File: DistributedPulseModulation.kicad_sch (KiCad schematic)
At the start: 43 parts, among them J1 Conn_02x12_Odd_Even, J2 Conn_02x05_Odd_Even, U1 74LS251, U10 4053, U11 4053, U12 4053, U2 74LVC2G74, U25 74LS85, U28 74LS85, U31 74LS85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

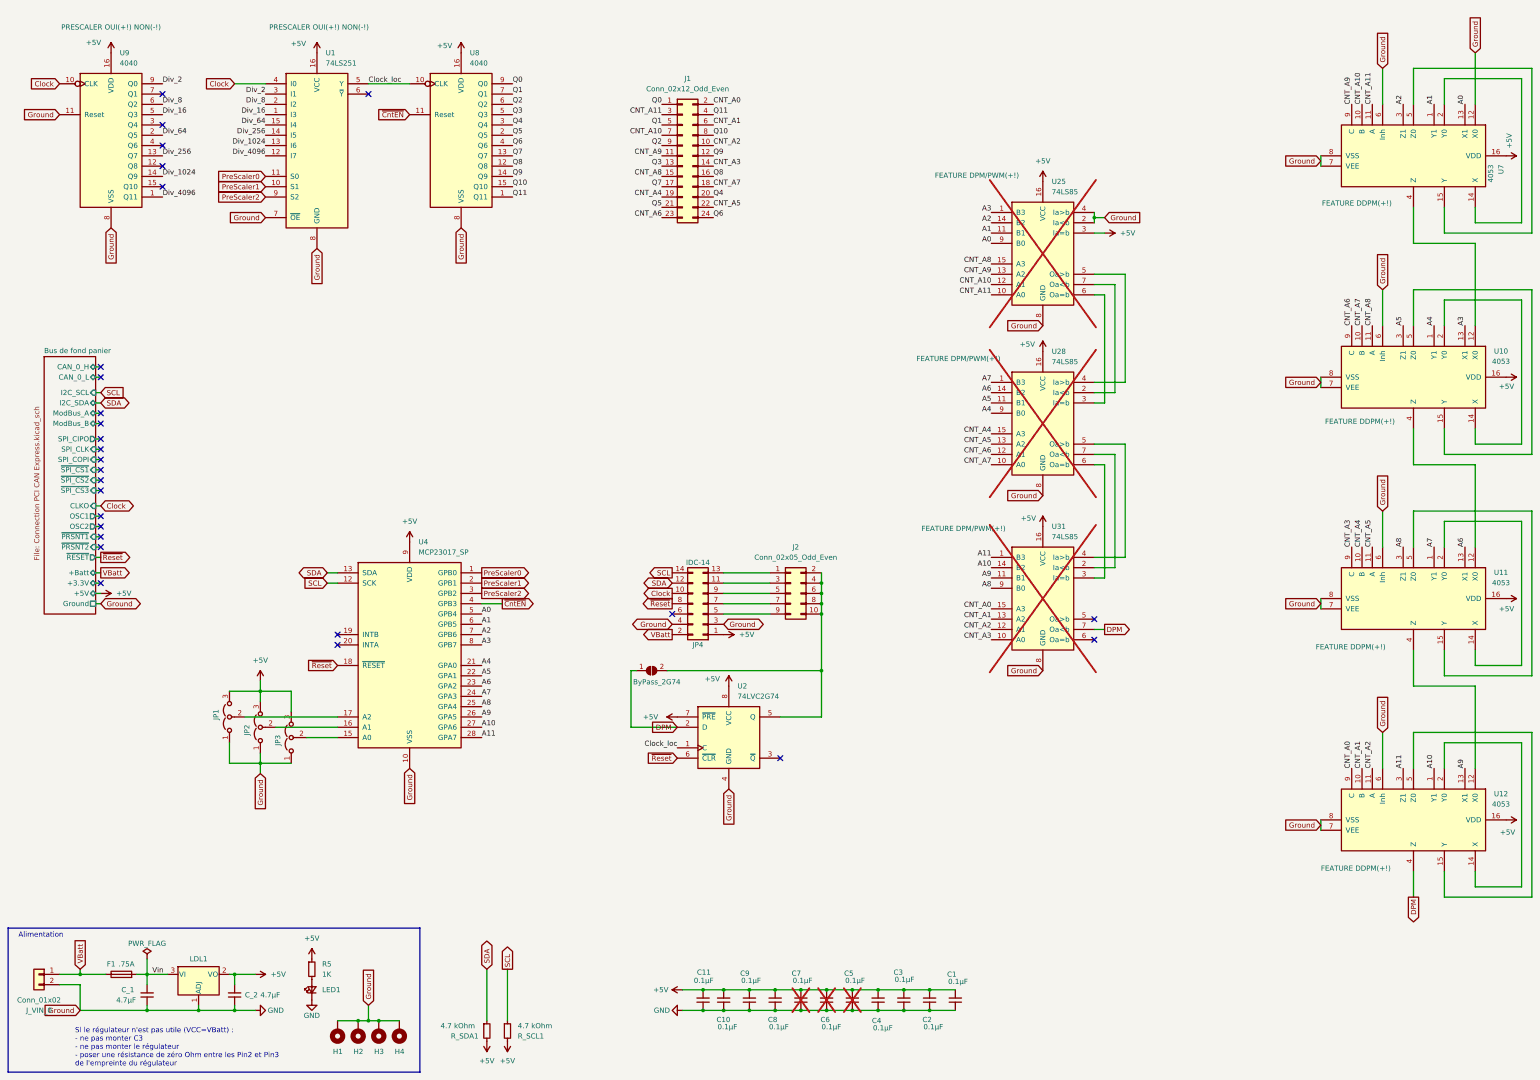
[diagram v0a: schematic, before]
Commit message: Feature : - DPM et DDPM sur même position de jumper - PWM sur jumpers en croisés
KiVar :
- création des 4 aspects FULL, PWM, DPM et DDPM

Doc/img :
- mise à jour du README.md
- mise à jour des screeshots
- intégration directe dans le projet des modèles 3D
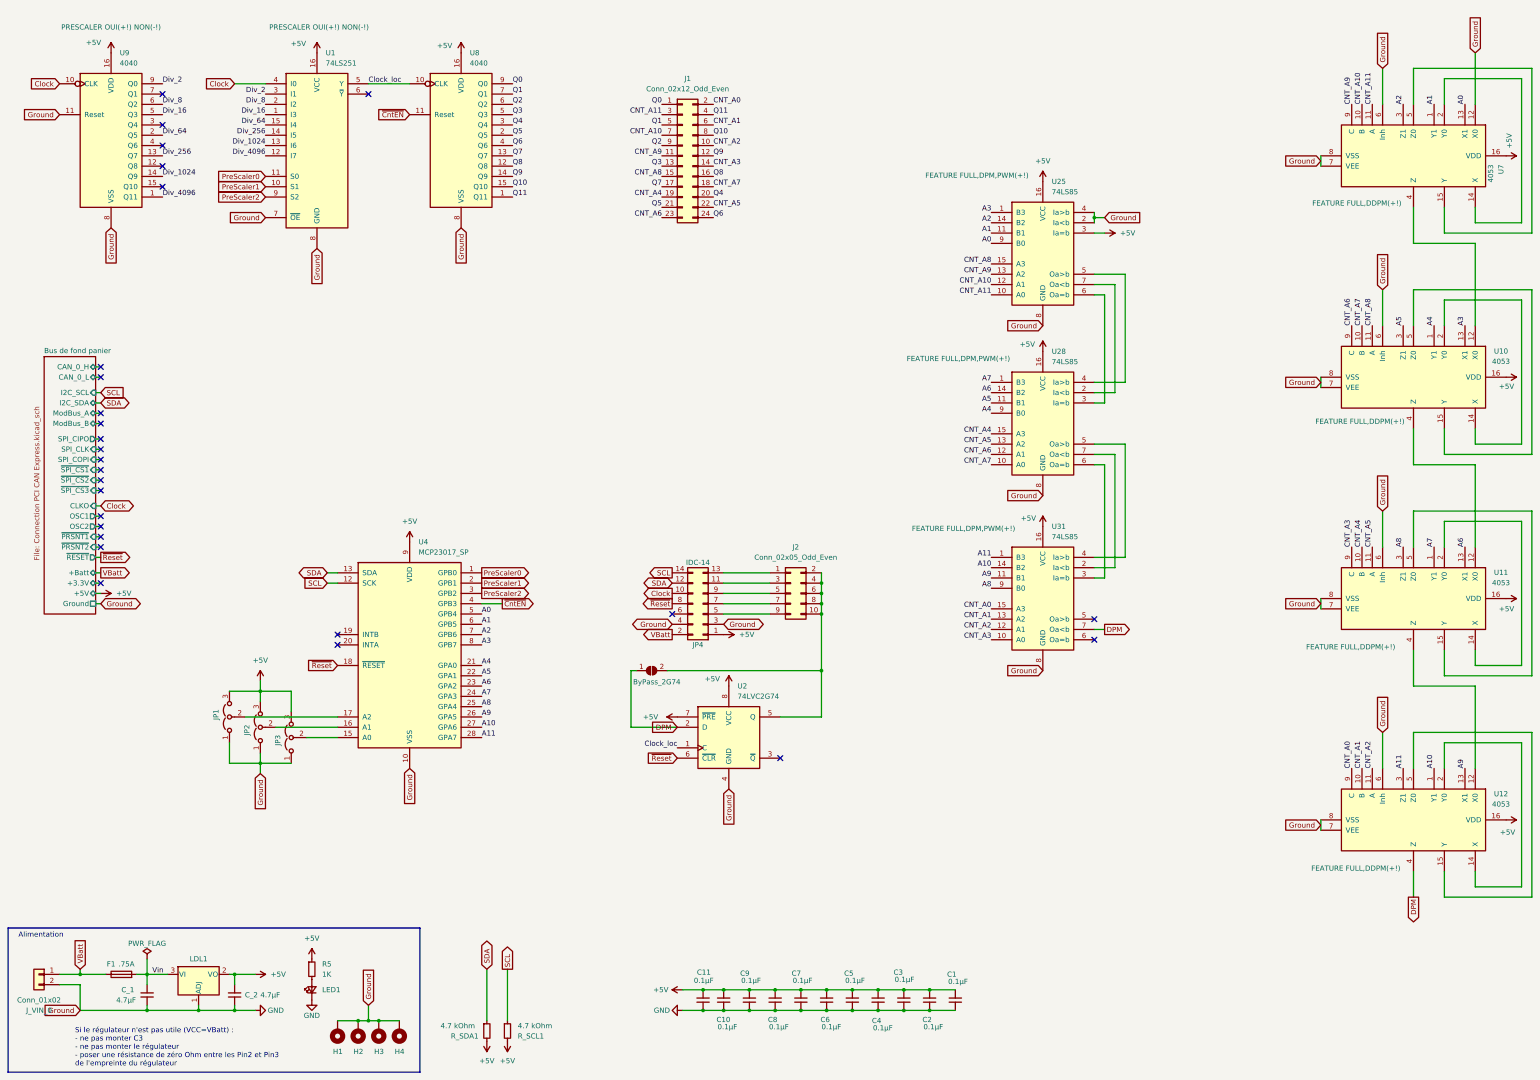
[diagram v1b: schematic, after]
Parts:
- C10, C11, C8, C9, U10, U11, U12, U7: Var FEATURE DDPM(+!) -> FEATURE FULL,DDPM(+!)
- C5, C6, C7, U25, U28, U31: Var FEATURE DPM/PWM(+!) -> FEATURE FULL,DPM,PWM(+!); now fitted; now in the parts list
- J1: Var (none) -> FEATURE FULL(+m1) DDPM,DPM(+m2) PWM(+m3)

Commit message: Travaux préparatoire : V2.0 - Ajout jumper Dyadic vs P82C150 - B.Silkscreen major update
TODO :
- Suppression connecteur IDC
- Ajout pinheader horizontal pour les 5 outputs
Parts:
- added JP5: Jumper_3_Open, Connector_PinHeader_2.54mm:PinHeader_1x03_P2.54mm_Vertical, symbol Jumper:Jumper_3_Open
- J1: Var FEATURE FULL(+m1) DDPM,DPM(+m2) PWM(+m3) -> FEATURE PWM(+m1) FULL,DDPM,DPM(+m2)
- J_VIN_0: footprint Connector_PinHeader_2.54mm:PinHeader_1x02_P2.54mm_Vertical -> TerminalBlock_TE-Connectivity:TerminalBlock_TE_282834-2_1x02_P2.54mm_Horizontal
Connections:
- net DPM: no longer names the net of ByPass_2G74.1 (A), U2.2 (D)
- net DPM: now also JP5.2 (C); no longer U12.4 (Z), U31.7 (Oa<b)
- new net DDPM: JP5.1 (A), U12.4 (Z)
- new net DPM_PWM: JP5.3 (B), U31.7 (Oa<b)

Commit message: Pré-version de la v2.0
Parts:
- removed J2: Conn_02x05_Odd_Even, Connector_PinHeader_2.54mm:PinHeader_2x05_P2.54mm_Vertical, symbol Connector_Generic:Conn_02x05_Odd_Even
- removed JP4: IDC-14, Connector_IDC:IDC-Header_2x07_P2.54mm_Horizontal, symbol Connector_Generic:Conn_02x07_Odd_Even
- added J2: Conn_01x01, Connector_PinSocket_2.54mm:PinSocket_1x01_P2.54mm_Horizontal, symbol Connector_Generic:Conn_01x01
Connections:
- net DPM: now reaches ByPass_2G74.2 (B), U2.5 (Q)
- net DPM: now also J2.1 (Pin_1)
- no-connect marks 27 -> 26

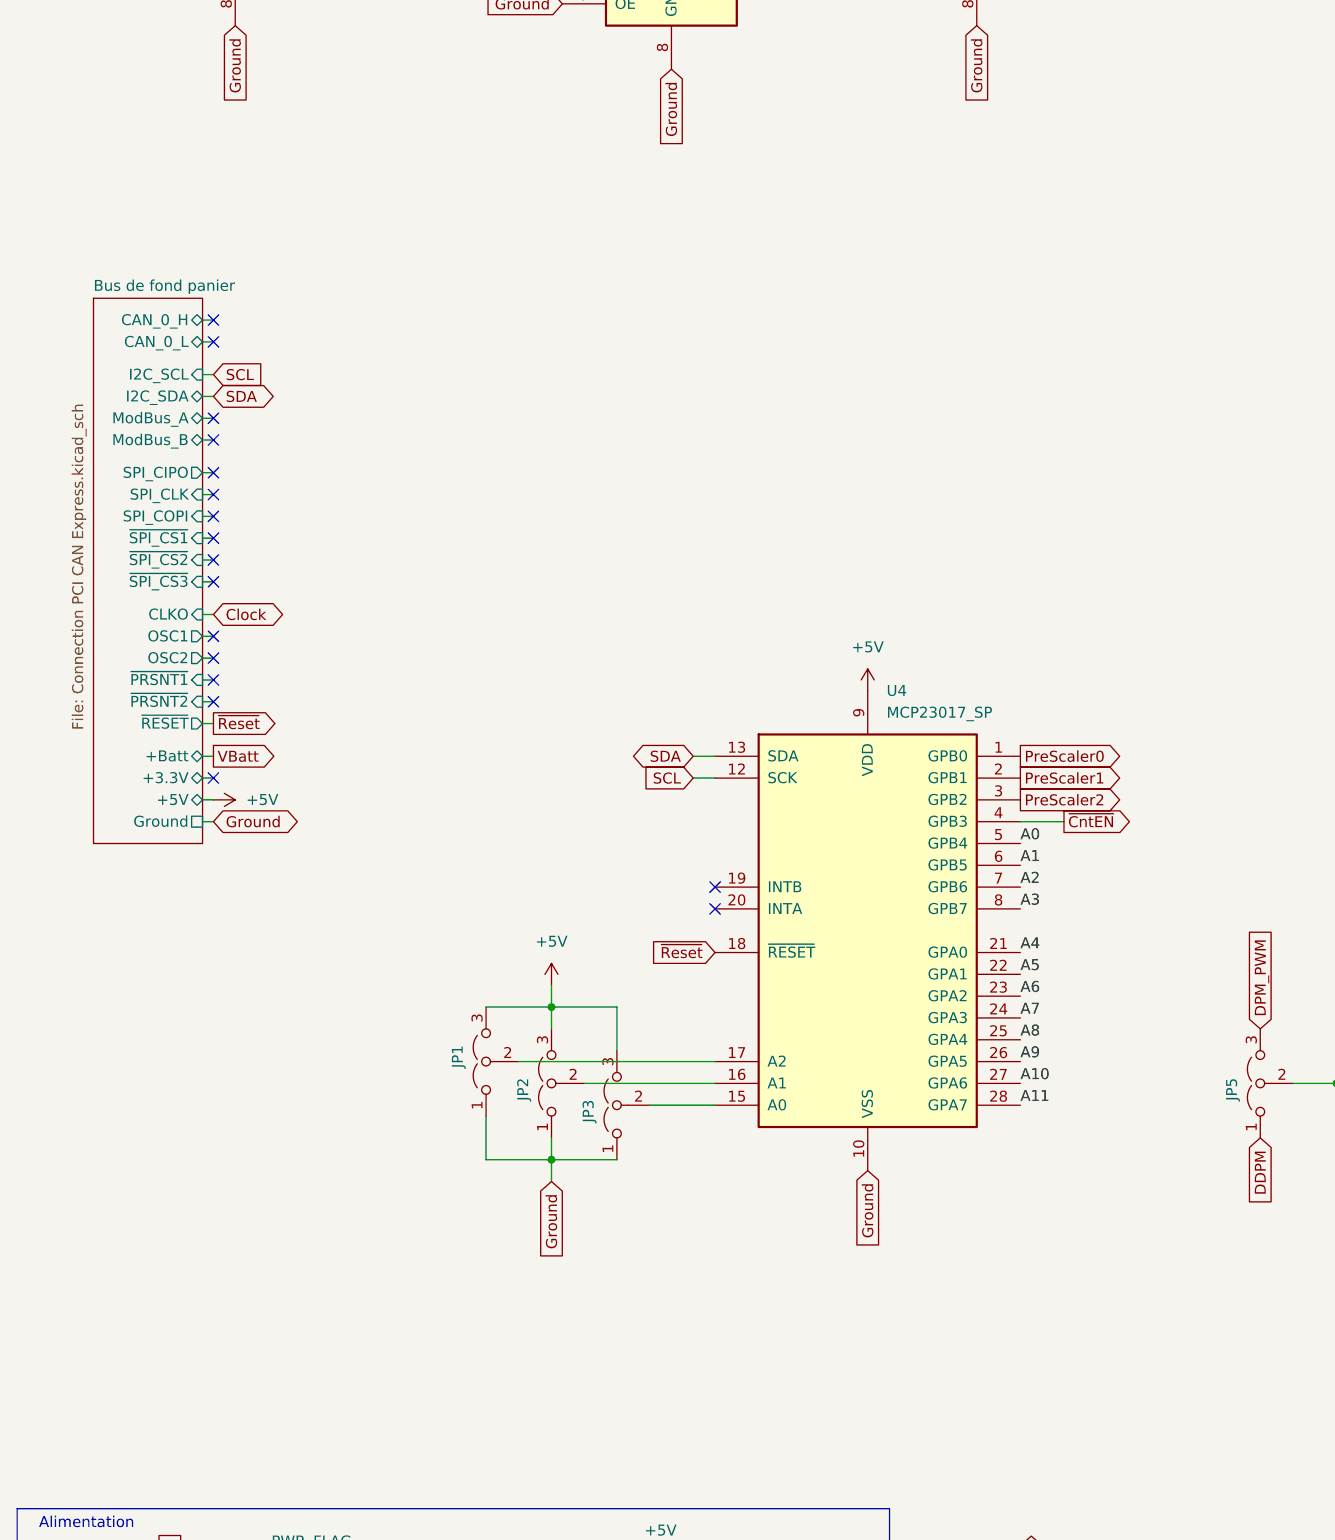
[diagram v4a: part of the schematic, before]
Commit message: Ajout test-points pour les ports A et B du MCP23017 Léger reroutage
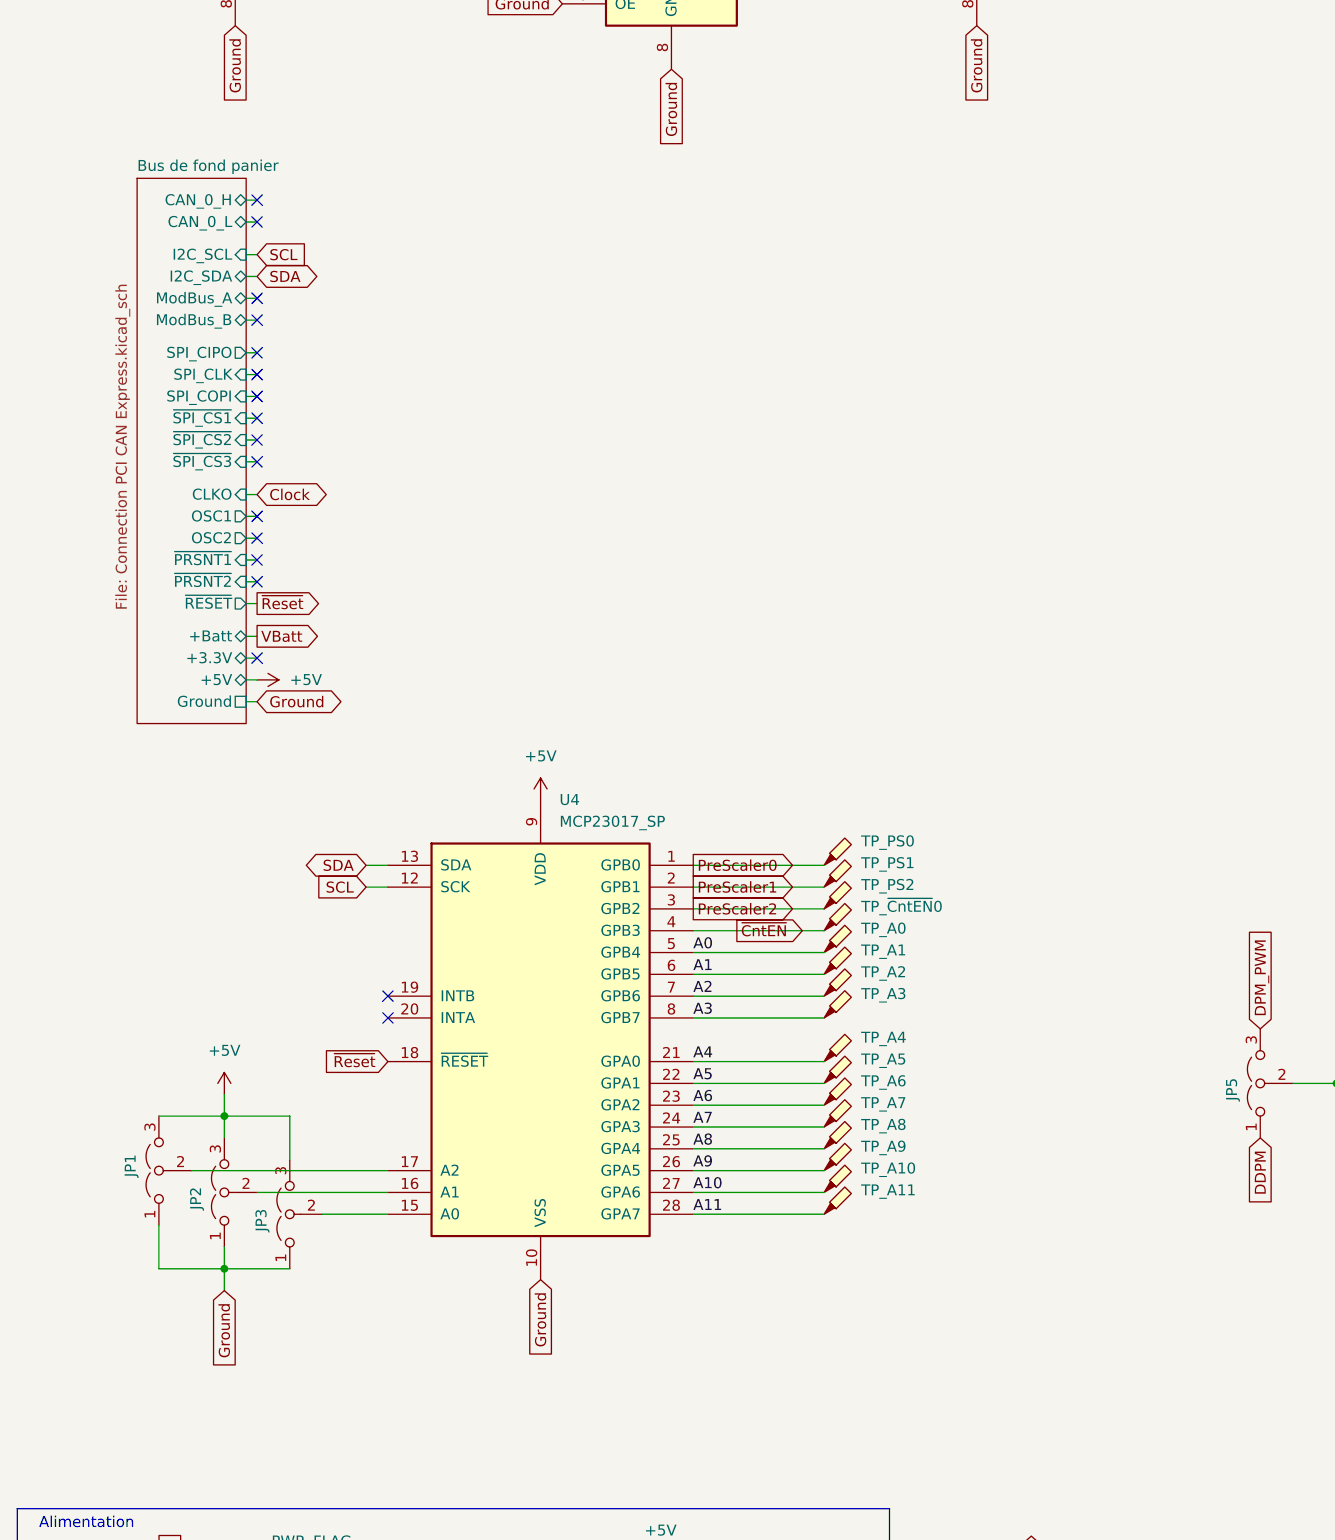
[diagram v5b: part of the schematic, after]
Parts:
- added TP_A0, TP_A1, TP_A10, TP_A11, TP_A2, TP_A3, TP_A4, TP_A5, TP_A6, TP_A7, TP_A8, TP_A9, TP_PS0, TP_PS1, TP_PS2, TP_~{CntEN}0: TestPoint_Probe, TestPoint:TestPoint_Pad_D1.5mm, symbol Connector:TestPoint_Probe
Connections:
- net A0: now also TP_A0.1
- net A1: now also TP_A1.1
- net A10: now also TP_A10.1
- net A11: now also TP_A11.1
- net A2: now also TP_A2.1
- net A3: now also TP_A3.1
- net A4: now also TP_A4.1
- net A5: now also TP_A5.1
- net A6: now also TP_A6.1
- net A7: now also TP_A7.1
- net A8: now also TP_A8.1
- net A9: now also TP_A9.1
- net PreScaler0: now also TP_PS0.1
- net PreScaler1: now also TP_PS1.1
- net PreScaler2: now also TP_PS2.1
- net ~{CntEN}: now also TP_~{CntEN}0.1
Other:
- moved on the sheet: JP1, JP2, JP3, U4
